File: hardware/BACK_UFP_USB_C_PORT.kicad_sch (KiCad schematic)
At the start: 27 parts, among them J7 USB4200-03-A (VIRT FLAG MOUNT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, Q18 PMPB09R5VPX, Q19 PMPB09R5VPX, Q20 PMPB09R5VPX, Q21 PMPB09R5VPX, U13 USB5926C, U3 PTN110NHQZ

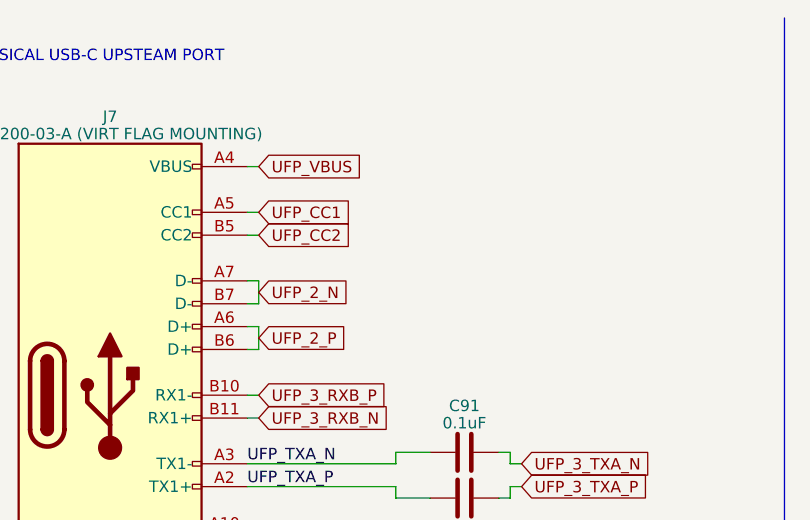
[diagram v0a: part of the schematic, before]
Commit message: updated block digram minor pcb changes
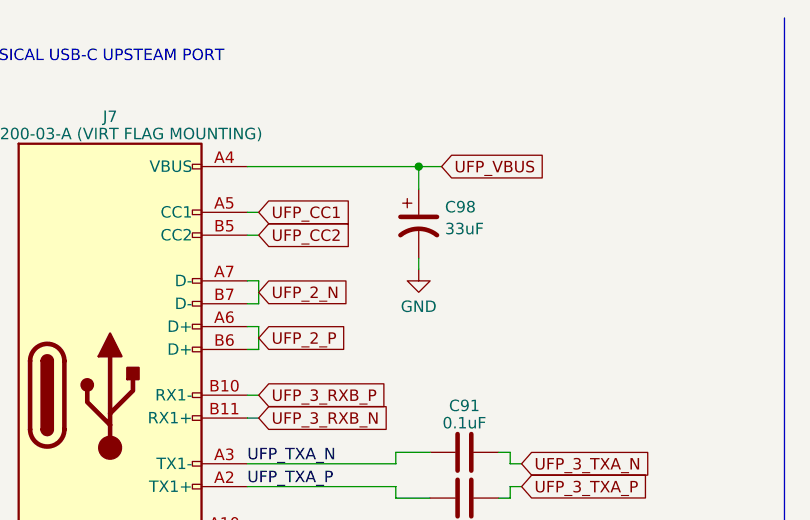
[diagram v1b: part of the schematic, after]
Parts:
- added C98: 33uF, Capacitor_SMD:C_Elec_6.3x5.8, symbol Device:C_Polarized_US
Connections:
- net GND: now also C98.2
- net UFP_VBUS: now also C98.1

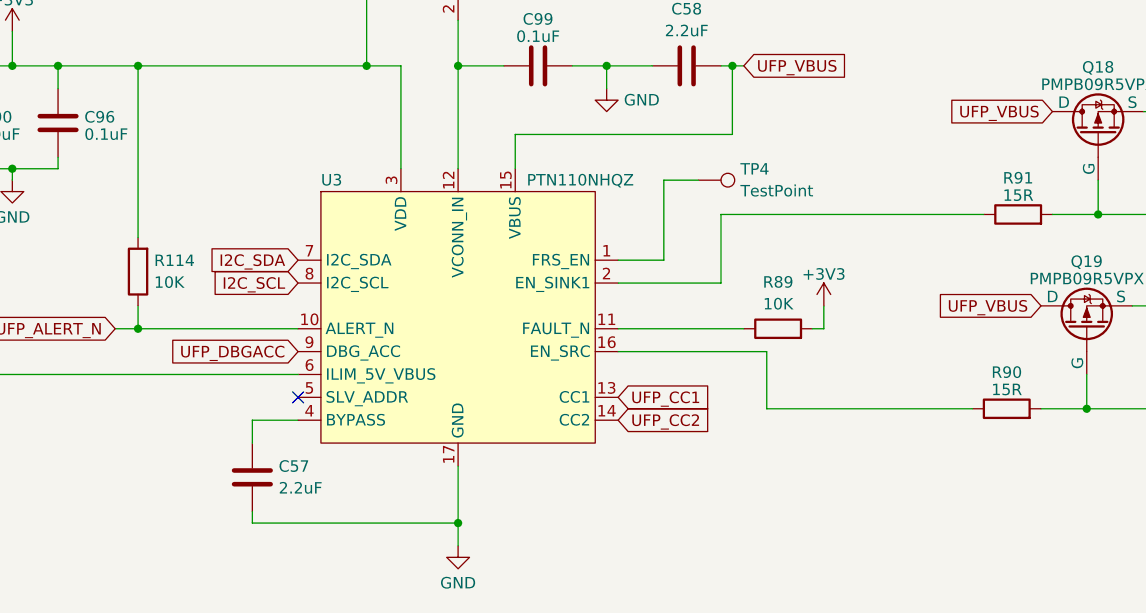
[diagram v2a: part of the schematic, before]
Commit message: switched can tranceiver to combo controler and tranceiver
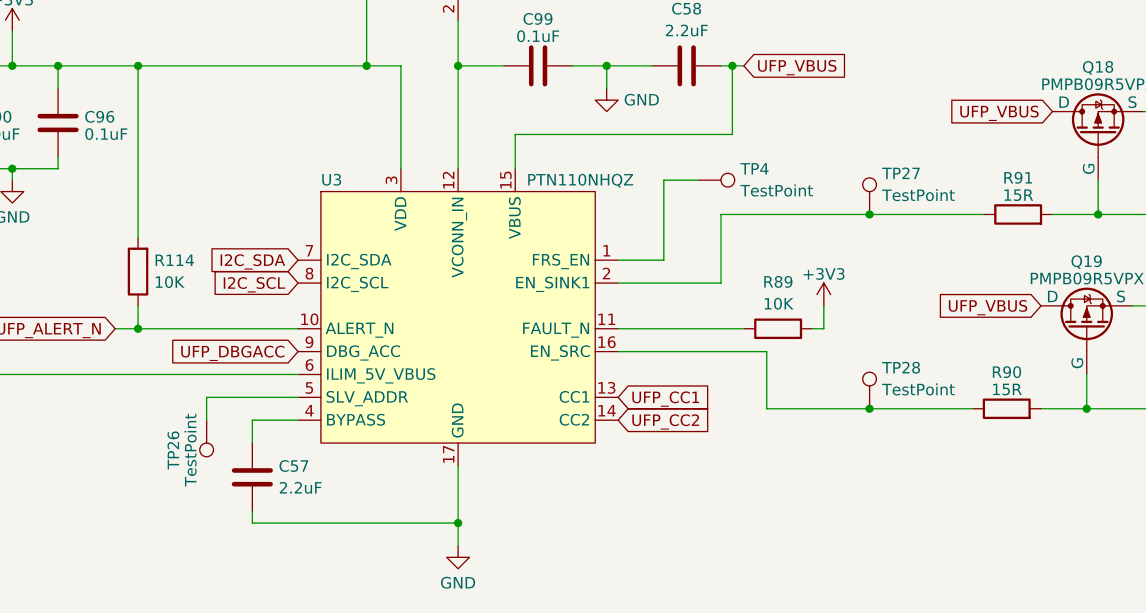
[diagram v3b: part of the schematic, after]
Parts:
- added TP26, TP27, TP28: TestPoint, TestPoint:TestPoint_Pad_D1.0mm, symbol Connector:TestPoint
- TP21, TP4: footprint TestPoint:TestPoint_Pad_D1.5mm -> TestPoint:TestPoint_Pad_D1.0mm
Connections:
- net at R91.1, U3.2 (EN_SINK1): now also TP27.1
- net at R90.1, U3.16 (EN_SRC): now also TP28.1
- net at U3.5 (SLV_ADDR): now also TP26.1
- no-connect marks 3 -> 2

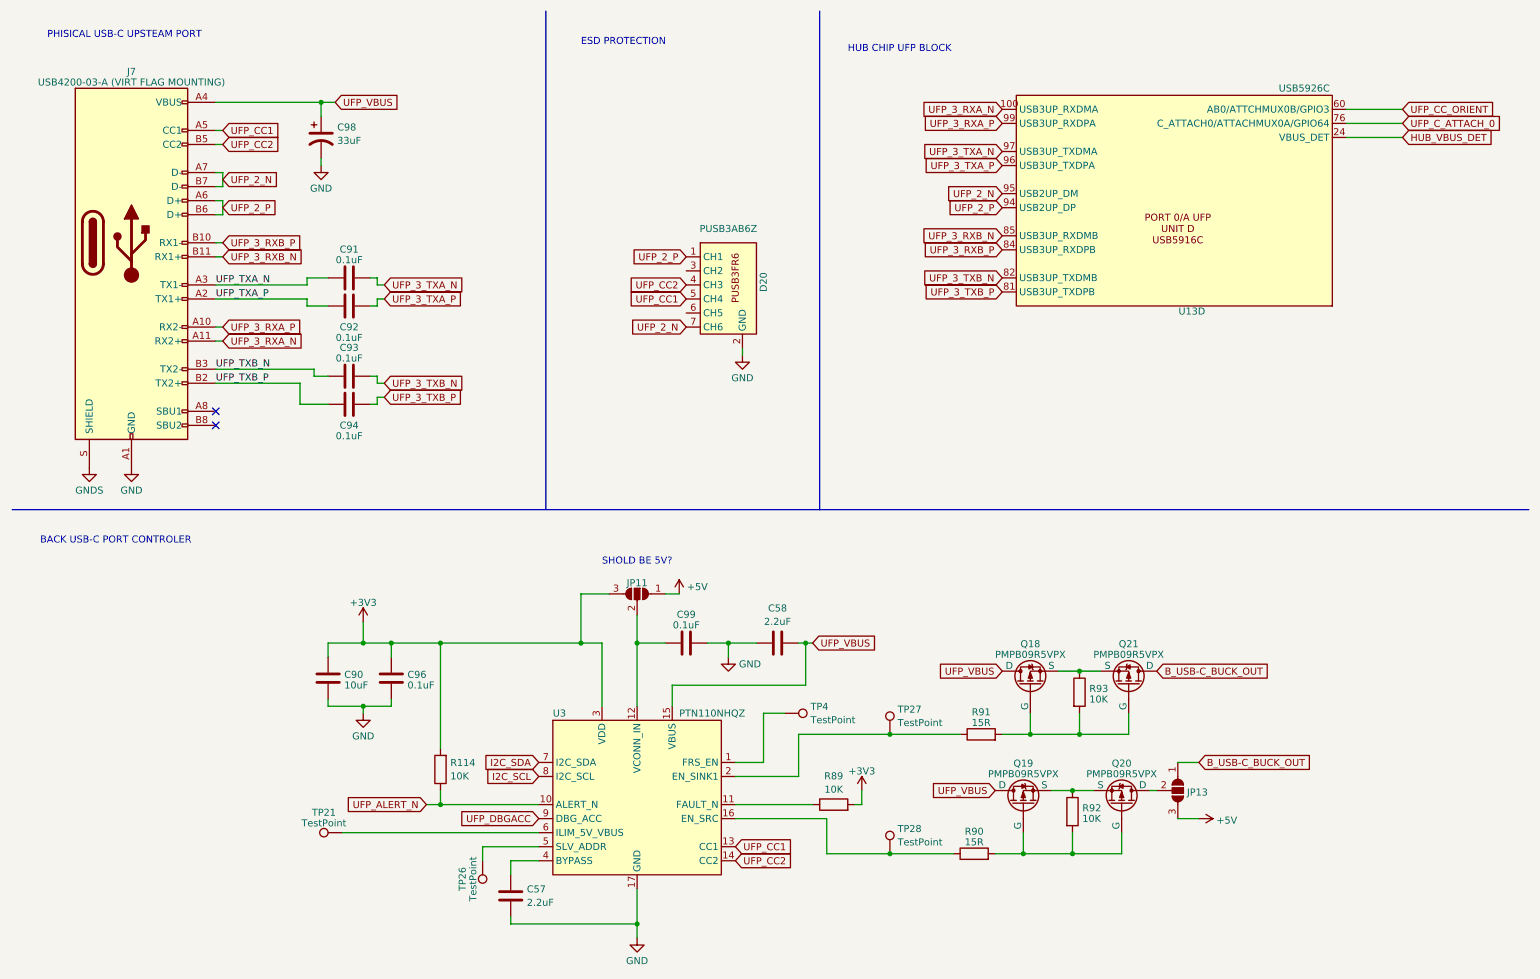
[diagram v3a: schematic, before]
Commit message: migrated to the esp32-s2 and starting new board revison
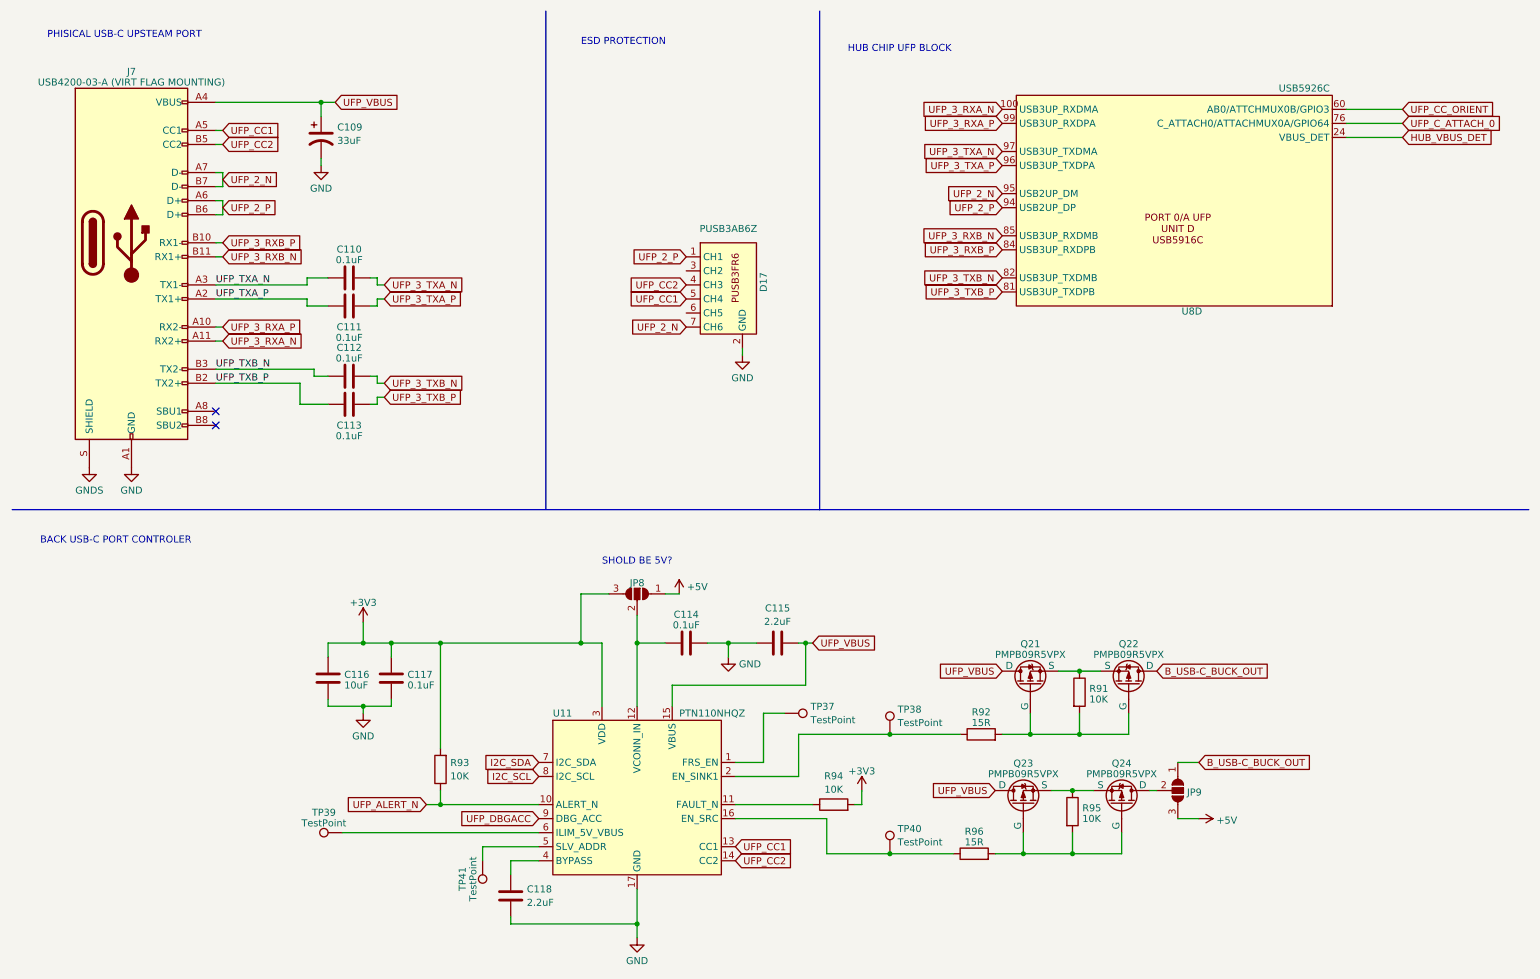
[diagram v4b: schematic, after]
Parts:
- renumbered C98 to C109, C91 to C110, C92 to C111, C93 to C112, C94 to C113, C99 to C114, C58 to C115, C90 to C116, C96 to C117, C57 to C118, D20 to D17, JP11 to JP8, JP13 to JP9, Q18 to Q21, Q21 to Q22, Q19 to Q23, Q20 to Q24, R93 to R91, R91 to R92, R114 to R93, R89 to R94, R92 to R95, R90 to R96, TP4 to TP37, TP27 to TP38, TP21 to TP39, TP28 to TP40, TP26 to TP41, U3 to U11, U13 to U8
